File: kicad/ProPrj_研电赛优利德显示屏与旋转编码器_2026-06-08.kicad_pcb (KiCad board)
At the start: 2 copper layers, 45 x 75 mm, 16 parts, among them Q1 S8050, SW1 EC11N1525405, U1 ST7789_12P_LCD

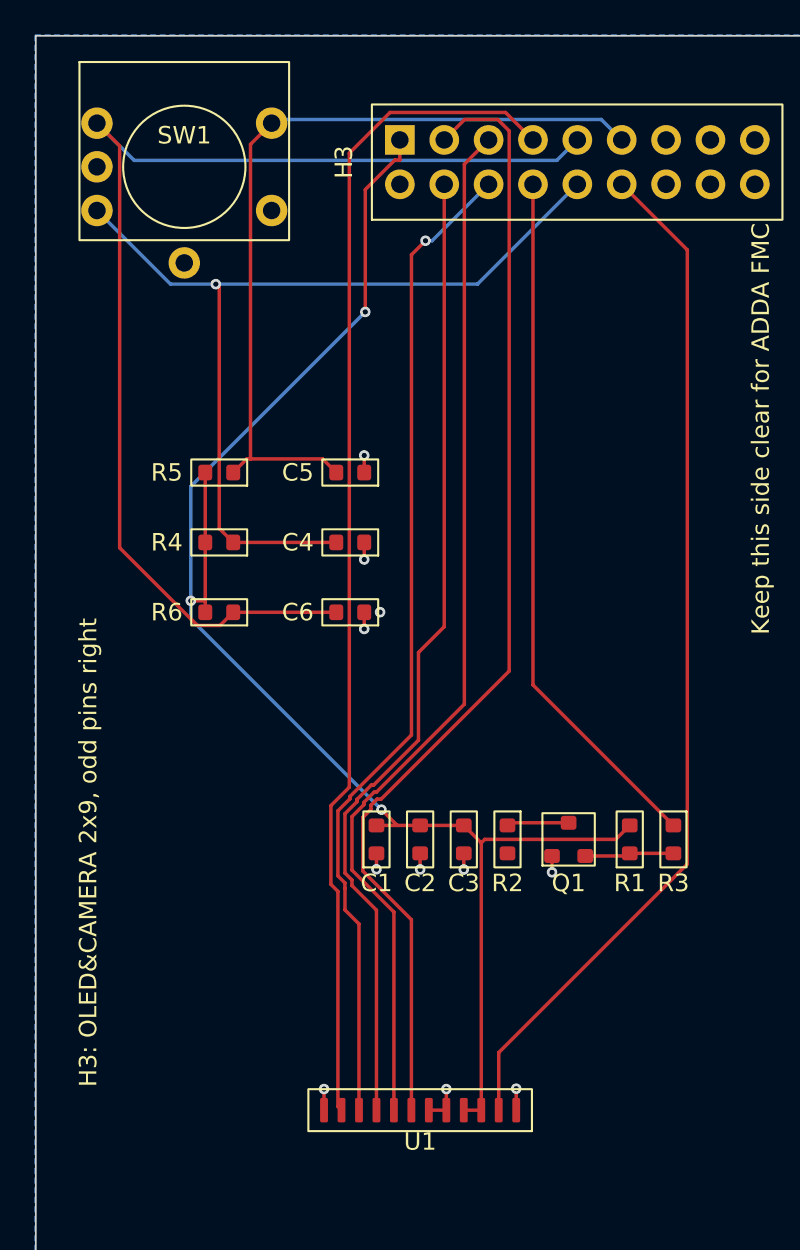
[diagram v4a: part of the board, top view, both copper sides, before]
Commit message: docs: rewrite architecture doc and fix old paths
- Rewrite 顶层架构图.md: remove transitional bring-up content,
  reflect current architecture with all verified modules
- Fix 19 hardcoded old paths (D:\awg_fpga, D:\FPGA\...) in
  顶层架构图.md and AD9144 Bring-Up.md
- Update docs/modules/* references to relative paths

Co-Authored-By: Claude Opus 4.8 <noreply@anthropic.com>
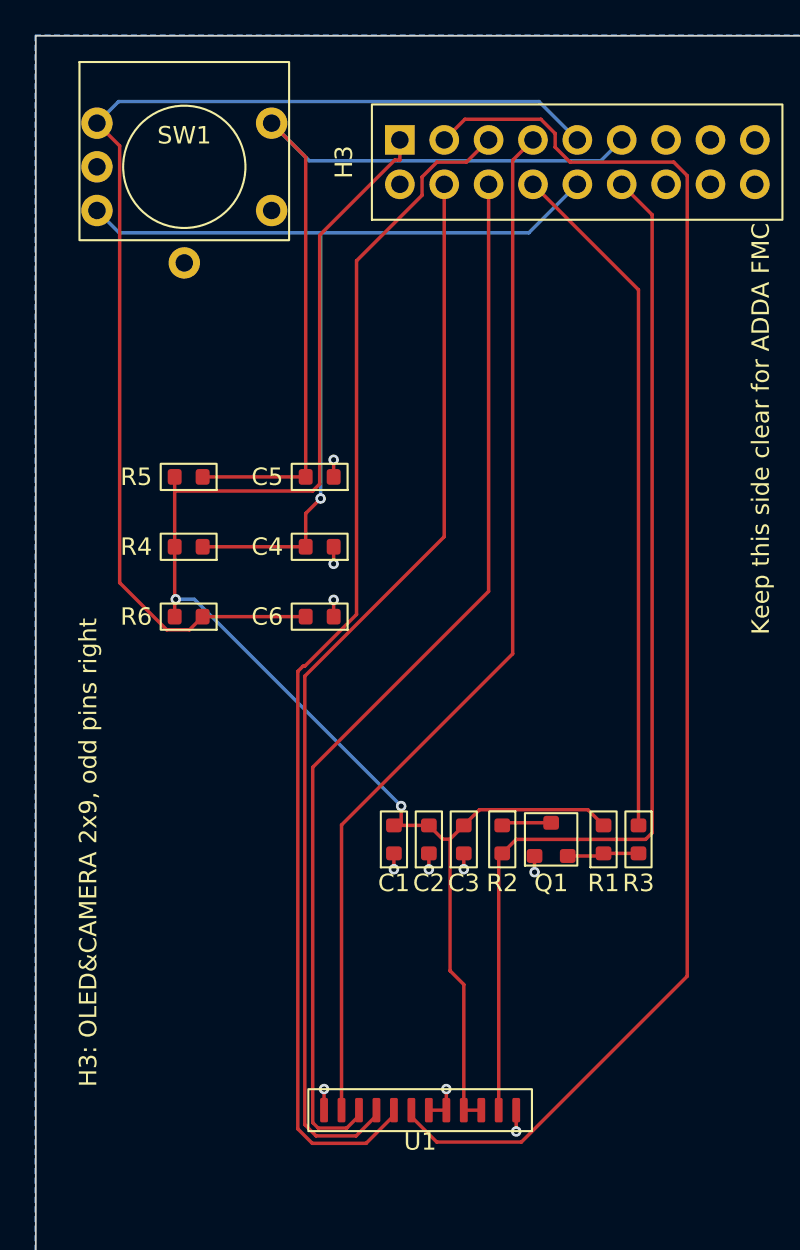
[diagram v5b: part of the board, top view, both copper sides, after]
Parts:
- C1, C2, C3, C4, C5, C6: footprint ProPrj_研电赛-easyedapro:C0603 -> design_lib:C0603
- H3: footprint ProPrj_研电赛-easyedapro:HDR-TH_18P-P2.54-V-M-R2-C9-S2.54 -> design_lib:HDR-TH_18P-P2.54-V-M-R2-C9-S2.54
- Q1: footprint ProPrj_研电赛-easyedapro:SOT-23-3_L2.9-W1.3-P1.90-LS2.4-BR -> design_lib:SOT-23-3_L2.9-W1.3-P1.90-LS2.4-BR
- R1, R2, R3, R4, R5, R6: footprint ProPrj_研电赛-easyedapro:R0603 -> design_lib:R0603
- SW1: footprint ProPrj_研电赛-easyedapro:EC11_ROTARY_ENCODER -> design_lib:EC11_ROTARY_ENCODER
- U1: footprint ProPrj_研电赛-easyedapro:ST7789_12P_1x12_1.00mm -> design_lib:ST7789_12P_1x12_1.00mm
- moved R3 2.00 mm to (109.0, 85.0)
- moved C4 1.77 mm to (90.8, 68.2)
- moved C5 1.77 mm to (90.8, 64.2)
- moved C6 1.77 mm to (90.8, 72.2)
- moved R4 1.77 mm to (83.2, 68.2)
- moved R5 1.77 mm to (83.2, 64.2)
- moved R6 1.77 mm to (83.2, 72.2)
- moved R1 1.50 mm to (107.0, 85.0)
- moved C1 1.00 mm to (95.0, 85.0)
- moved Q1 1.00 mm to (104.0, 85.0)
- moved C2 0.50 mm to (97.0, 85.0)
- moved R2 0.30 mm to (101.2, 85.0)
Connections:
- R2 pad 2: /LEDK -> LEDK
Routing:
- net TFT_DC: track 65.3 -> 82.7 mm
- net TFT_CS: track 59.9 -> 69.0 mm
- net TFT_RES: track 67.6 -> 60.1 mm
- net TFT_SCL: track 56.2 -> 62.3 mm
- net TFT_SDA: track 57.3 -> 61.3 mm, vias 1 -> 0
- net LEDK: track 59.0 -> 61.7 mm
- net VCC: track 89.7 -> 87.4 mm, vias 3 -> 2
- net EC11-M: track 46.9 -> 48.4 mm
- net Net-(Q1-B): track 5.11 -> 4.11 mm
- net TFT_BLK: track 40.0 -> 39.2 mm
- net Net-(Q1-C): track 3.56 -> 2.86 mm
- net EC11-B: track 52.7 -> 53.4 mm
- net GND: track 11.3 -> 11.2 mm, vias 11 -> 10

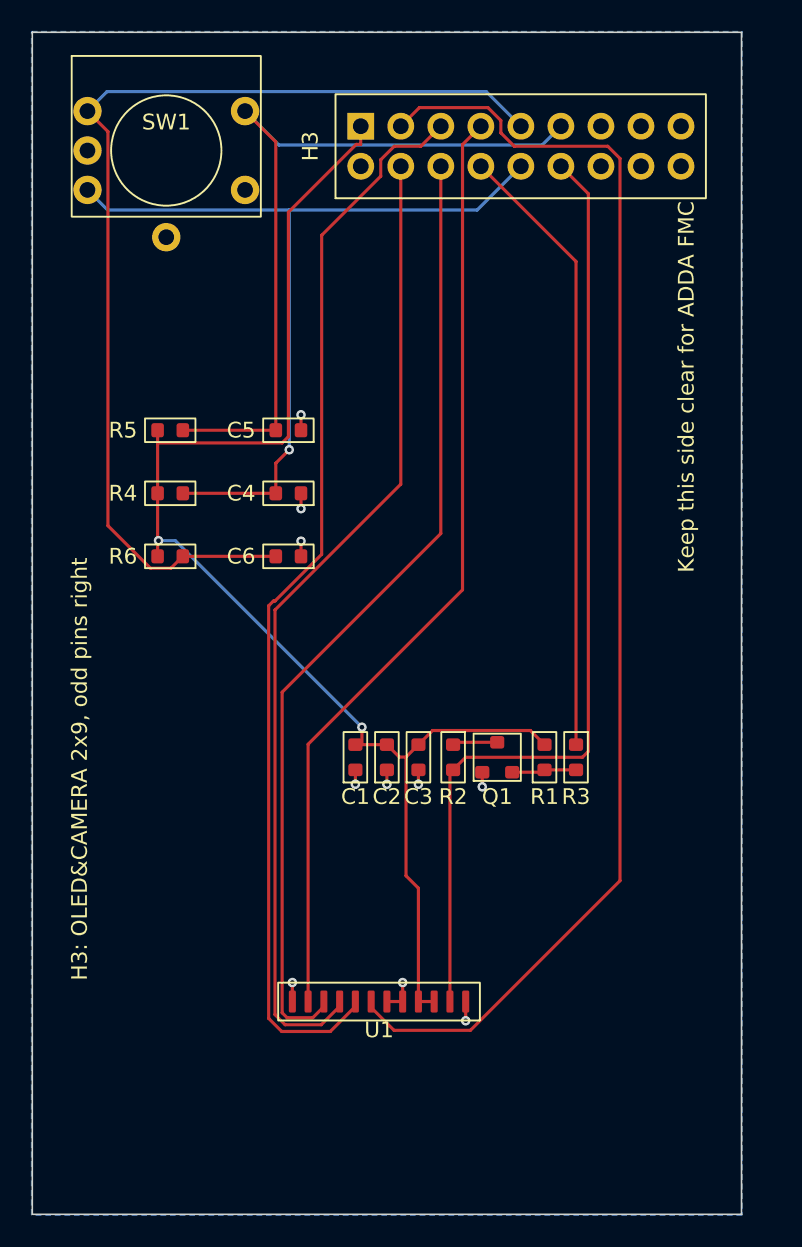
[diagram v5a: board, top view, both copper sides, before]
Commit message: feat: enable UART control in build
- Add verilog_define AWG_UART_CONTROL=1 to build scripts
- UART 115200 8N1 on w_tx_core_clk (250MHz)
- Pins: T22 (txd), T23 (rxd) LVCMOS33
- Enables remote register access via ad9144_uart_reg_bridge

Co-Authored-By: Claude Opus 4.8 <noreply@anthropic.com>
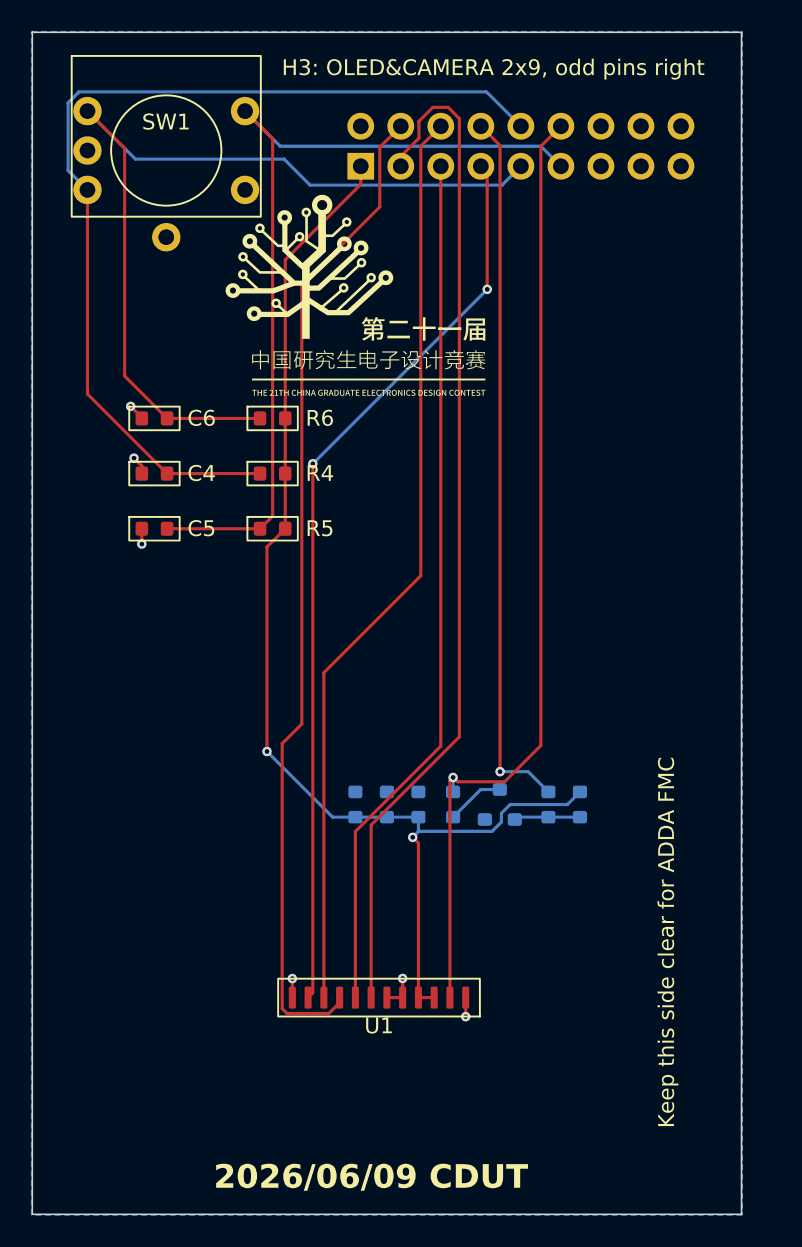
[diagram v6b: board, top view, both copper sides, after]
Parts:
- C1, C2, C3, H3, Q1, R1, R2, R3: moved to B.Cu
- moved C6 12.2 mm to (82.2, 63.5), turned to 0 degrees
- moved R6 10.9 mm to (89.8, 63.5), turned to 0 degrees
- moved C5 10.6 mm to (82.2, 70.5), turned to 0 degrees
- moved R5 9.02 mm to (89.8, 70.5), turned to 0 degrees
- moved C4 8.59 mm to (82.2, 67.0), turned to 0 degrees
- moved R4 6.62 mm to (89.8, 67.0), turned to 0 degrees
- moved R1 3.75 mm to (109.2, 88.0)
- moved R3 3.47 mm to (107.2, 88.0)
- moved Q1 3.00 mm to (104.2, 88.0), turned to -90 degrees
- moved C1 3.00 mm to (95.0, 88.0), turned to -90 degrees
- moved C2 3.00 mm to (97.0, 88.0), turned to -90 degrees
- moved C3 3.00 mm to (99.0, 88.0), turned to -90 degrees
- moved R2 3.00 mm to (101.2, 88.0), turned to 90 degrees
- moved U1 0.25 mm to (96.5, 100.2)
- turned H3 to -90 degrees
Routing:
- net TFT_DC: track 82.7 -> 64.6 mm
- net TFT_CS: track 69.0 -> 55.0 mm
- net VCC: track 87.4 -> 75.3 mm
- net EC11-A: track 67.8 -> 57.4 mm
- net EC11-B: track 53.4 -> 61.9 mm, vias 1 -> 0
- net EC11-M: track 48.4 -> 54.9 mm
- net TFT_BLK: track 39.2 -> 45.1 mm, vias 0 -> 1
- net GND: track 11.2 -> 7.84 mm, vias 10 -> 6
- net TFT_SDA: track 61.3 -> 58.4 mm
- net TFT_RES: track 60.1 -> 57.6 mm, vias 0 -> 2
- net TFT_SCL: track 62.3 -> 63.5 mm
- net Net-(Q1-C): track 2.86 -> 3.69 mm
- net LEDK: track 61.7 -> 61.4 mm, vias 0 -> 1
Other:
- board text added: "2026/06/09 CDUT"
